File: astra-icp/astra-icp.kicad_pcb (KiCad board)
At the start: 2 copper layers, 180 x 56 mm, 71 parts, among them IC1 ATA6561-GAQW-N, J1 SWD, J2 PWR_IN, J3 CAN_TERMINAL, J4 UART, SW1 CHOC_HS, SW10 CHOC_HS, SW11 CHOC_HS, SW12 CHOC_HS, SW13 CHOC_HS, SW14 CHOC_HS, SW15 CHOC_HS, SW16 CHOC_HS, SW17 CHOC_HS, SW18 CHOC_HS, SW19 CHOC_HS, SW2 CHOC_HS, SW20 CHOC_HS, SW3 CHOC_HS, SW4 CHOC_HS, SW5 CHOC_HS, SW6 CHOC_HS, SW7 CHOC_HS, SW8 CHOC_HS, SW9 CHOC_HS, U3 STM32F042C4Tx

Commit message: fix: More tweaks for real component choice
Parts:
- D1, D10, D11, D12, D13, D14, D15, D16, D17, D18, D19, D2, D20, D3, D4, D5, D6, D7, D8, D9: footprint PCM_Diode_SMD_AKL:D_0603_1608Metric_Pad1.05x0.95mm_HandSolder -> Diode_SMD:D_SOD-323
- R10, R11, R9: value 15 -> 60.4
- R13: value 145 -> 130
- R14: value 60.4 -> 45

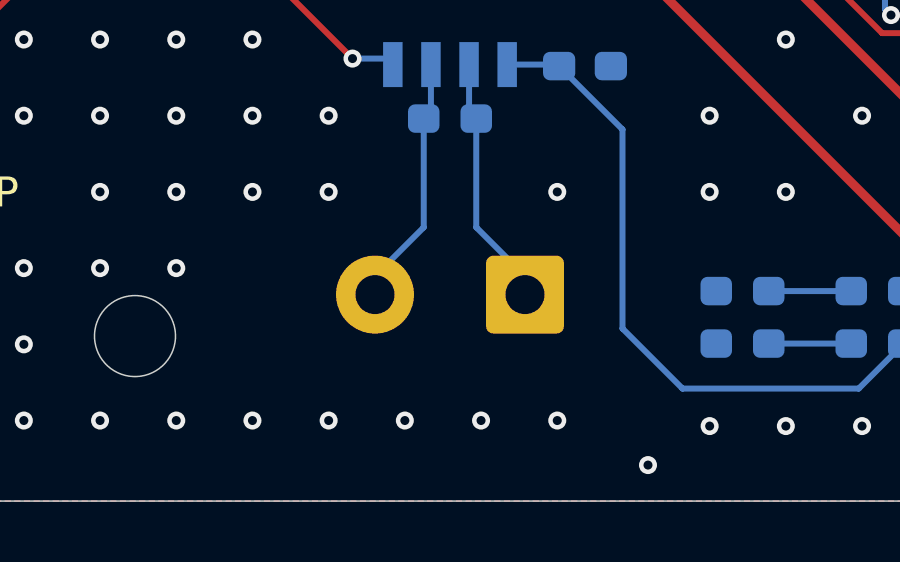
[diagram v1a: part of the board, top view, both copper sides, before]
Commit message: Changed CAN connector in ICP
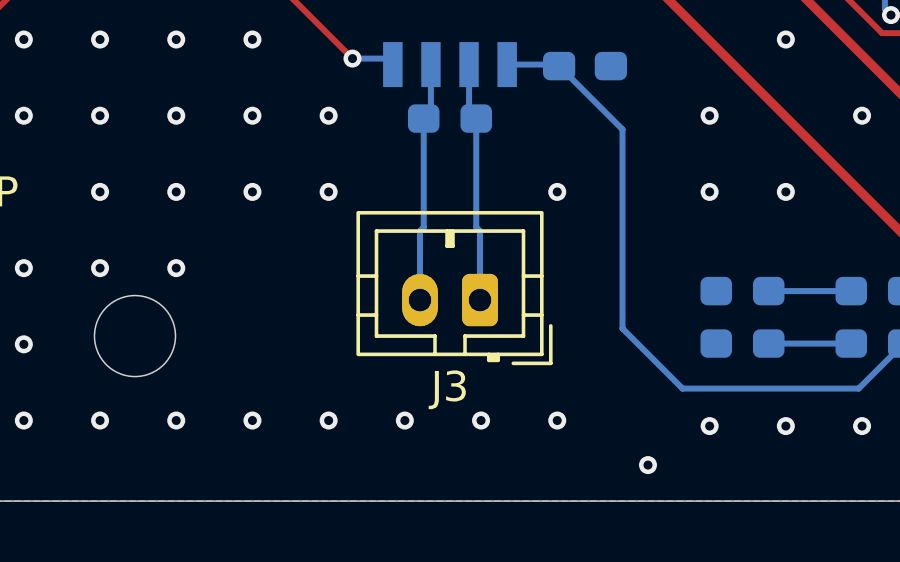
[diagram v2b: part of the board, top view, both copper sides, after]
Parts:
- J3: value CAN_TERMINAL -> CAN_CONN; footprint TerminalBlock_Phoenix:TerminalBlock_Phoenix_PT-1,5-2-5.0-H_1x02_P5.00mm_Horizontal -> Connector_JST:JST_PH_B2B-PH-K_1x02_P2.00mm_Vertical; moved to F.Cu
- R14: value 45 -> 47
- moved J3 1.51 mm to (124.0, 71.3)
